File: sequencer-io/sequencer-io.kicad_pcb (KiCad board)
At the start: 2 copper layers, 156.5 x 89.8 mm, 96 parts, among them SW1 SW_Push, SW10 SW_Push, SW11 SW_Push, SW12 SW_Push, SW13 SW_Push, SW14 SW_Push, SW15 SW_Push, SW16 SW_Push, SW17 SW_Push, SW18 SW_Push, SW19 SW_Push, SW2 SW_Push, SW20 SW_Push, SW21 SW_Push, SW22 SW_Push, SW23 SW_Push, SW24 RotaryEncoder, SW3 SW_Push, SW4 SW_Push, SW5 SW_Push, SW6 SW_Push, SW7 SW_Push, SW8 SW_Push, SW9 SW_Push, U2 74HC595

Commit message: Edited PCB
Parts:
- added D24: 1N4148W, Diode_SMD:D_SOD-323_HandSoldering, B.Cu at (178.5, 115.5)
- added U20: SC0915, SC0915:SC0915, B.Cu at (155.8, 129.6)
- C10, C11, C12, C13, C14, C15, C16, C17, C18, C19, C20, C4, C5, C6, C7, C8, C9, U10, U11, U12, U13, U14, U15, U16, U17, U18, U19, U3, U4, U5, U6, U7, U8, U9: moved to B.Cu
- moved C13 173.3 mm to (38.1, 71.2), turned to 180 degrees
- moved C12 172.8 mm to (38.1, 90.5), turned to 180 degrees
- moved C14 154.6 mm to (57.1, 71.2), turned to 180 degrees
- moved C11 153.9 mm to (57.1, 90.5), turned to 180 degrees
- moved U3 138.7 mm to (171.5, 105.0), turned to 180 degrees
- moved C15 136.0 mm to (76.2, 71.2), turned to 180 degrees
- moved C10 135.1 mm to (76.2, 90.5), turned to 180 degrees
- moved C16 120.1 mm to (95.2, 71.2), turned to 180 degrees
- moved U4 115.3 mm to (171.4, 81.0), turned to 180 degrees
- moved U10 115.2 mm to (57.1, 81.0), turned to 180 degrees
- moved C9 111.2 mm to (95.2, 90.5), turned to 180 degrees
- moved C17 101.3 mm to (114.3, 71.2), turned to 180 degrees
- moved C8 92.2 mm to (114.3, 90.5), turned to 180 degrees
- moved C18 82.7 mm to (133.3, 71.2), turned to 180 degrees
- moved U9 77.6 mm to (76.2, 81.0), turned to 180 degrees
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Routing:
- net +5V: track 0.00 -> 616.1 mm, vias 0 -> 21
- net DIGIT_3: track 0.00 -> 267.2 mm
- net DIGIT_2: track 0.00 -> 261.2 mm
- net DIGIT_1: track 0.00 -> 246.4 mm
- net ENC_B: track 7.47 -> 200.8 mm
- net ENC_A: track 7.47 -> 197.7 mm
- net ROW1: track 133.4 -> 277.4 mm
- net ROW0: track 57.2 -> 164.7 mm
- net COL0: track 132.9 -> 238.0 mm, vias 0 -> 1
- net ROW3: track 128.4 -> 208.9 mm
- net COL3: track 105.1 -> 182.2 mm, vias 0 -> 1
- net ROW2: track 133.3 -> 209.5 mm
- net COL1: track 146.3 -> 213.3 mm, vias 0 -> 1
- net COL4: track 19.0 -> 85.8 mm, vias 0 -> 1
- net COL5: track 19.0 -> 70.7 mm, vias 0 -> 1
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- added copper zone on B.Cu, net GND
- added copper zone on F.Cu, net GND
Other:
- board size 156.5 x 89.8 mm -> 157 x 117 mm

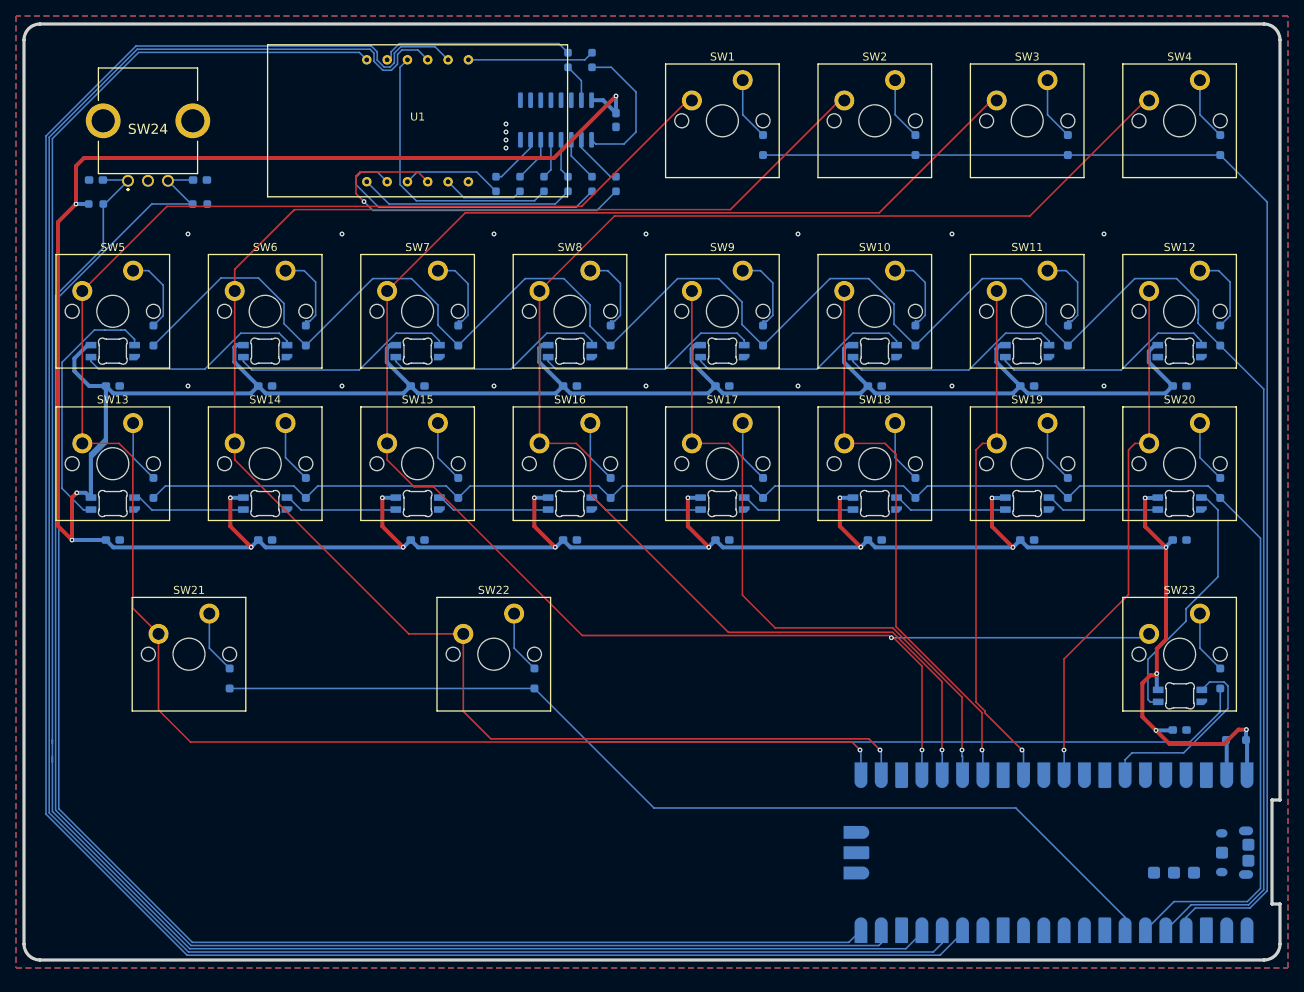
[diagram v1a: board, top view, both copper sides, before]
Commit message: Added TCA8418
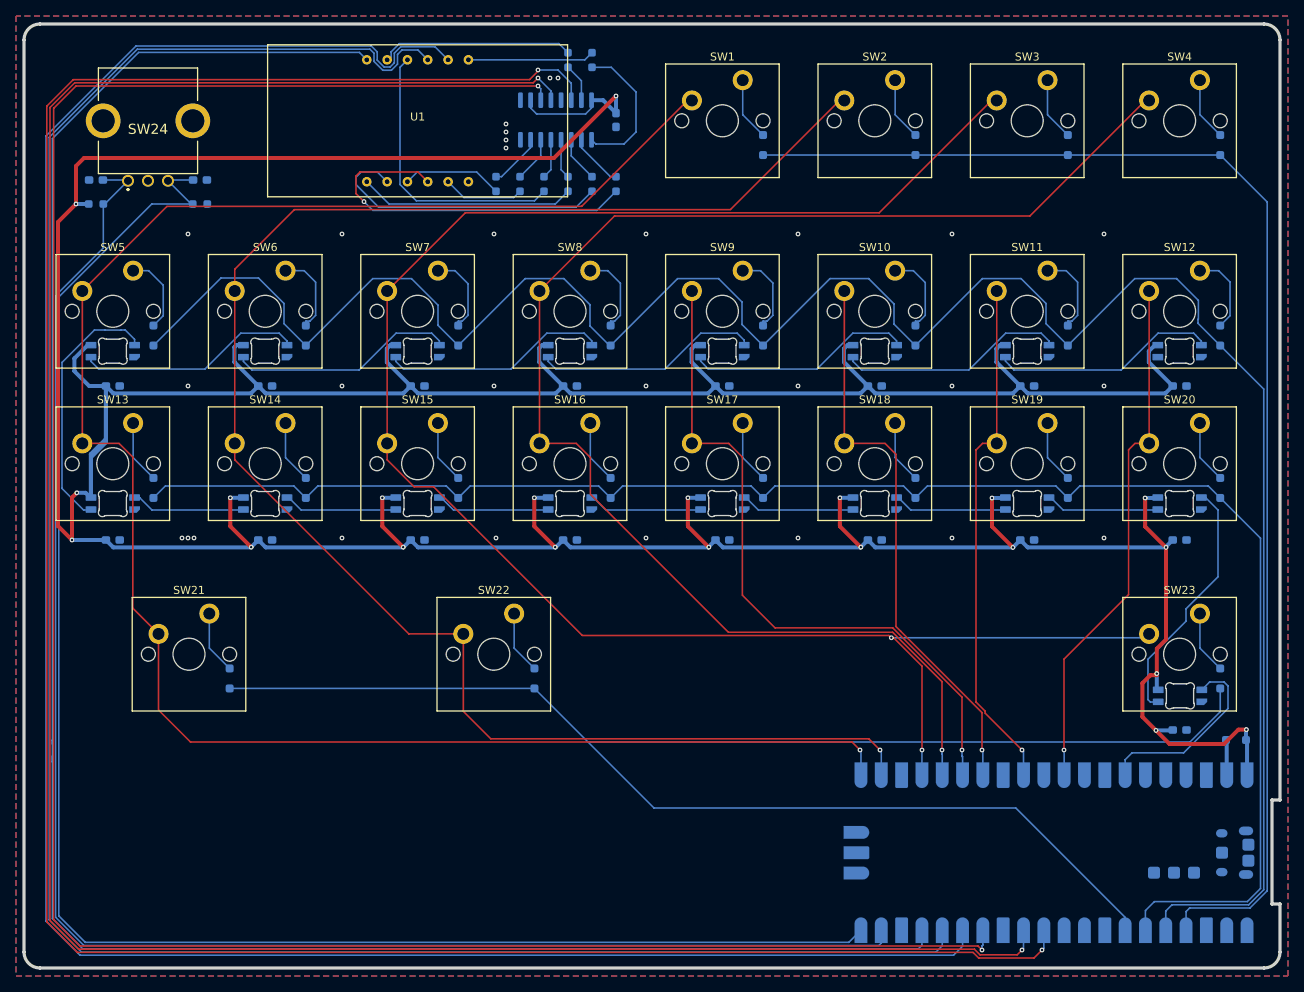
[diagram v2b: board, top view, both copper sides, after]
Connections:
- U2 pad 10: unconnected-(U2-~{SRCLR}-Pad10) -> +5V
- U2 pad 11: unconnected-(U2-SRCLK-Pad11) -> SRCLK
- U2 pad 12: unconnected-(U2-RCLK-Pad12) -> RCLK
- U2 pad 13: unconnected-(U2-~{OE}-Pad13) -> GND
- U2 pad 14: unconnected-(U2-SER-Pad14) -> SER
- U20 pad 11: unconnected-(U20-GP8-Pad11) -> SER
- U20 pad 12: unconnected-(U20-GP9-Pad12) -> RCLK
- U20 pad 14: unconnected-(U20-GP10-Pad14) -> SRCLK
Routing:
- net SER: track 0.00 -> 301.5 mm, vias 0 -> 2
- net RCLK: track 0.00 -> 293.7 mm, vias 0 -> 2
- net SRCLK: track 0.00 -> 285.2 mm, vias 0 -> 2
- net +5V: track 616.1 -> 626.3 mm
- net DIGIT_3: track 267.2 -> 276.0 mm
- net DIGIT_1: track 246.4 -> 255.2 mm
- net DIGIT_2: track 261.2 -> 269.2 mm
- net ENC_B: track 200.8 -> 208.7 mm
- net ENC_A: track 197.7 -> 205.5 mm
- net ROW2: track 209.5 -> 210.9 mm
- net ROW1: track 277.4 -> 278.8 mm
- net GND: vias 18 -> 29
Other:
- board size 157 x 117 mm -> 157 x 118 mm

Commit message: Added gitignore
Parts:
- added D25: BAT85, Package_TO_SOT_SMD:SOT-323_SC-70_Handsoldering, F.Cu at (133.5, 172.1)
- added D26: GATE, LED_THT:LED_D3.0mm_FlatTop, F.Cu at (126.3, 172.8)
- added J1: GateOut, Connector_PinHeader_2.54mm:PinHeader_1x02_P2.54mm_Vertical, F.Cu at (117.8, 165.2)
- added J2: ClockOut, Connector_PinHeader_2.54mm:PinHeader_1x02_P2.54mm_Vertical, F.Cu at (122.4, 165.2)
- added J3: PitchOut, Connector_PinHeader_2.54mm:PinHeader_1x02_P2.54mm_Vertical, F.Cu at (127.0, 165.2)
- added J4: CVOut, Connector_PinHeader_2.54mm:PinHeader_1x02_P2.54mm_Vertical, F.Cu at (131.7, 165.2)
- added J5: ClockIn, Connector_PinHeader_2.54mm:PinHeader_1x02_P2.54mm_Vertical, F.Cu at (136.3, 165.2)
- added J6: ResetIn, Connector_PinHeader_2.54mm:PinHeader_1x02_P2.54mm_Vertical, F.Cu at (141.0, 165.2)
- added Q1: MMBT3904, Package_TO_SOT_SMD:SOT-23, F.Cu at (122.2, 172.5)
- added Q2: MMBT3904, Package_TO_SOT_SMD:SOT-23, F.Cu at (122.2, 177.1)
- added R11: 1k, Resistor_SMD:R_0603_1608Metric_Pad0.98x0.95mm_HandSolder, F.Cu at (117.6, 171.3)
- added R12: 1k, Resistor_SMD:R_0603_1608Metric_Pad0.98x0.95mm_HandSolder, F.Cu at (117.6, 173.8)
- added R13: 100k, Resistor_SMD:R_0603_1608Metric_Pad0.98x0.95mm_HandSolder, F.Cu at (117.6, 176.4)
- added R14: 1M, Resistor_SMD:R_0603_1608Metric_Pad0.98x0.95mm_HandSolder, F.Cu at (117.6, 178.9)
- added R15: 10k, Resistor_SMD:R_0603_1608Metric_Pad0.98x0.95mm_HandSolder, F.Cu at (117.6, 181.4)
- added R16: 10k, Resistor_SMD:R_0603_1608Metric_Pad0.98x0.95mm_HandSolder, F.Cu at (117.6, 183.9)
- added R17: 100k, Resistor_SMD:R_0603_1608Metric_Pad0.98x0.95mm_HandSolder, F.Cu at (117.6, 186.4)
- added R18: 1M, Resistor_SMD:R_0603_1608Metric_Pad0.98x0.95mm_HandSolder, F.Cu at (117.6, 188.9)
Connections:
- U20 pad 1: unconnected-(U20-GP0-Pad1) -> GATE
- U20 pad 10: unconnected-(U20-GP7-Pad10) -> CV
- U20 pad 2: unconnected-(U20-GP1-Pad2) -> CLKOUT
- U20 pad 9: unconnected-(U20-GP6-Pad9) -> PITCH

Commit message: lil update
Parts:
- added C21: 100nF, Capacitor_SMD:C_0603_1608Metric_Pad1.08x0.95mm_HandSolder, F.Cu at (222.2, 76.9)
- added C22: 100nF, Capacitor_SMD:C_0603_1608Metric_Pad1.08x0.95mm_HandSolder, F.Cu at (222.2, 49.8)
- added C23: 22pF, Capacitor_SMD:C_0603_1608Metric_Pad1.08x0.95mm_HandSolder, F.Cu at (222.2, 52.3)
- added C24: 22pF, Capacitor_SMD:C_0603_1608Metric_Pad1.08x0.95mm_HandSolder, F.Cu at (222.2, 54.8)
- added C25: 100nF, Capacitor_SMD:C_0603_1608Metric_Pad1.08x0.95mm_HandSolder, F.Cu at (222.2, 57.3)
- added D27: SS34F, Diode_SMD:D_SMA_Handsoldering, F.Cu at (212.8, 61.0)
- added D28: 1SMB5918BT3G, Diode_SMD:D_SMB_Handsoldering, F.Cu at (212.8, 66.5)
- added IC1: TCA8418RTWR, Package_DFN_QFN:QFN-24-1EP_4x4mm_P0.5mm_EP2.5x2.5mm, B.Cu at (113.6, 105.2)
- added J7: ResetIn, Connector_PinHeader_2.54mm:PinHeader_1x02_P2.54mm_Vertical, F.Cu at (226.7, 77.9)
- added Q3: MMBT3906, Package_TO_SOT_SMD:SOT-23, F.Cu at (200.8, 60.6)
- added Q4: MMBT3906, Package_TO_SOT_SMD:SOT-23, F.Cu at (200.8, 65.2)
- added Q5: MMBT3904, Package_TO_SOT_SMD:SOT-23, F.Cu at (200.8, 69.8)
- added Q6: MMBT3904, Package_TO_SOT_SMD:SOT-23, F.Cu at (214.3, 99.4)
- added Q7: DMG2305UX-7, Package_TO_SOT_SMD:SOT-23, F.Cu at (226.9, 85.2)
- added R19: 680R, Resistor_SMD:R_0603_1608Metric_Pad0.98x0.95mm_HandSolder, F.Cu at (222.2, 79.4)
- added R20: 10k, Resistor_SMD:R_0603_1608Metric_Pad0.98x0.95mm_HandSolder, F.Cu at (222.2, 81.9)
- added R21: 1k, Resistor_SMD:R_0603_1608Metric_Pad0.98x0.95mm_HandSolder, B.Cu at (118.6, 108.4)
- added R22: 1k, Resistor_SMD:R_0603_1608Metric_Pad0.98x0.95mm_HandSolder, B.Cu at (121.6, 108.4)
- added R23: 100k, Resistor_SMD:R_0603_1608Metric_Pad0.98x0.95mm_HandSolder, F.Cu at (205.4, 59.5)
- added R24: 1M, Resistor_SMD:R_0603_1608Metric_Pad0.98x0.95mm_HandSolder, F.Cu at (205.4, 62.0)
- added R25: 10k, Resistor_SMD:R_0603_1608Metric_Pad0.98x0.95mm_HandSolder, F.Cu at (205.4, 64.5)
- added R26: 100k, Resistor_SMD:R_0603_1608Metric_Pad0.98x0.95mm_HandSolder, F.Cu at (205.4, 67.0)
- added R27: 1M, Resistor_SMD:R_0603_1608Metric_Pad0.98x0.95mm_HandSolder, F.Cu at (205.4, 69.5)
- added R28: 1k, Resistor_SMD:R_0603_1608Metric_Pad0.98x0.95mm_HandSolder, F.Cu at (222.2, 59.8)
- added R29: 10k, Resistor_SMD:R_0603_1608Metric_Pad0.98x0.95mm_HandSolder, F.Cu at (222.2, 62.3)
- added R30: 10k, Resistor_SMD:R_0603_1608Metric_Pad0.98x0.95mm_HandSolder, F.Cu at (222.2, 64.8)
- added R31: 1k, Resistor_SMD:R_0603_1608Metric_Pad0.98x0.95mm_HandSolder, F.Cu at (222.2, 67.3)
- added R32: 10k, Resistor_SMD:R_0603_1608Metric_Pad0.98x0.95mm_HandSolder, F.Cu at (222.2, 69.8)
- added R33: 10k, Resistor_SMD:R_0603_1608Metric_Pad0.98x0.95mm_HandSolder, F.Cu at (222.2, 72.3)
- added RV1: PITCH, Connector_PinHeader_2.54mm:PinHeader_1x03_P2.54mm_Vertical, F.Cu at (200.7, 50.8)
- added RV2: OCTAVE, Connector_PinHeader_2.54mm:PinHeader_1x03_P2.54mm_Vertical, F.Cu at (205.3, 50.8)
- added RV3: LENGTH, Connector_PinHeader_2.54mm:PinHeader_1x03_P2.54mm_Vertical, F.Cu at (210.0, 50.8)
- added RV4: CV, Connector_PinHeader_2.54mm:PinHeader_1x03_P2.54mm_Vertical, F.Cu at (214.6, 50.8)
- added TP1: TestPoint_Small, TestPoint:TestPoint_Pad_D1.0mm, B.Cu at (119.4, 111.6)
- added TP2: TestPoint_Small, TestPoint:TestPoint_Pad_D1.0mm, B.Cu at (117.2, 98.6)
- added TP3: TestPoint_Small, TestPoint:TestPoint_Pad_D1.0mm, B.Cu at (113.0, 111.6)
- added TP4: TestPoint_Small, TestPoint:TestPoint_Pad_D1.0mm, B.Cu at (114.0, 98.6)
- added TP5: TestPoint_Small, TestPoint:TestPoint_Pad_D1.0mm, B.Cu at (116.2, 111.6)
- added TP6: TestPoint_Small, TestPoint:TestPoint_Pad_D1.0mm, B.Cu at (109.8, 111.6)
- added U21: TL072, Package_SO:SOIC-8_3.9x4.9mm_P1.27mm, F.Cu at (228.6, 51.9)
- added U22: MCP4822, Package_SO:SOIC-8_3.9x4.9mm_P1.27mm, F.Cu at (228.6, 58.4)
- C1: value 100nF -> 47uF
- D1: value 1N4148W -> SS34F; footprint Diode_SMD:D_SOD-323_HandSoldering -> Diode_SMD:D_SMA_Handsoldering
- D25: value BAT85 -> 1SMB5918BT3G; footprint Package_TO_SOT_SMD:SOT-323_SC-70_Handsoldering -> Diode_SMD:D_SMB_Handsoldering
- J1: value GateOut -> 5V EXT
- J2: value ClockOut -> GateOut
- J3: value PitchOut -> ClockOut
- J4: value CVOut -> PitchOut
- J5: value ClockIn -> CVOut
- J6: value ResetIn -> ClockIn
- Q1: value MMBT3904 -> DMG2305UX-7
- Q2: value MMBT3904 -> MMBT3906
- R1, R2, R3, R4: value 100R -> 10k
- R10, R11, R12, R9: value 1k -> 100R
- R13: value 100k -> 100R
- R14: value 1M -> 100R
- R15, R16: value 10k -> 100R
- R17: value 100k -> 680R
- R18: value 1M -> 680R
- R5, R6, R7, R8: value 100R -> 1k
- U1: value ~ -> SC0915; footprint FJ5361BH:FJ5361BH -> SC0915:SC0915; moved to B.Cu
- U19: value ~ -> 74HC595; footprint SK6812MINI-E-012:SK6812MINI-E-012 -> Package_SO:SOIC-16_3.9x9.9mm_P1.27mm
- U2: value 74HC595 -> ~; footprint Package_SO:SOIC-16_3.9x9.9mm_P1.27mm -> SK6812MINI-E-012:SK6812MINI-E-012; moved to F.Cu
- U20: value SC0915 -> ~; footprint SC0915:SC0915 -> FJ5361BH:FJ5361BH
- moved D24 76.8 mm to (145.4, 184.8)
- moved U2 19.3 mm to (74.2, 38.0), turned to 0 degrees
- moved U1 17.2 mm to (93.4, 38.0), turned to 90 degrees
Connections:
- C2 pad 2: ENC_B -> +5V
- C20 pad 2: +5V -> /IOs/ENC_B
- C3 pad 2: ENC_A -> +5V
- D1 pad 1: ROW0 -> +5V
- D13 pad 1: ROW2 -> ROW1
- D21 pad 1: ROW3 -> ROW2
- D24 pad 1: /VSYS -> ROW3
- D24 pad 2: +5V -> Net-(D24-A)
- D25 pad 1: GATE -> /IOs/GATE
- D26 pad 2: GATE -> Net-(D26-A)
- D5 pad 1: ROW1 -> ROW0
- J1 pad 1: (no net) -> Net-(J1-Pin_1)
- J1 pad 2: (no net) -> GND
- Q1 pad 1: Net-(Q1-B) -> Net-(D1-A)
- Q1 pad 2: GND -> +5V
- Q1 pad 3: CLKIN -> Net-(J1-Pin_1)
- Q2 pad 2: GND -> +5V
- Q2 pad 3: RSTIN -> Net-(Q2-C)
- R1 pad 1: Net-(U2-QH) -> +3.3V
- R1 pad 2: Net-(U1-DP) -> /Switches/SDA
- R10 pad 1: +5V -> Net-(U19-QB)
- R10 pad 2: ENC_A -> Net-(U20-B)
- R11 pad 1: GATE -> Net-(U19-QC)
- R11 pad 2: Net-(J1-PadT) -> Net-(U20-C)
- R12 pad 1: GND -> Net-(U19-QD)
- R12 pad 2: Net-(D26-K) -> Net-(U20-D)
- R13 pad 1: Net-(J5-PadT) -> Net-(U19-QE)
- R13 pad 2: Net-(Q1-B) -> Net-(U20-E)
- R14 pad 1: GND -> Net-(U19-QF)
- R14 pad 2: Net-(Q1-B) -> Net-(U20-F)
- R15 pad 1: CLKIN -> Net-(U19-QG)
- R15 pad 2: +5V -> Net-(U20-G)
- R16 pad 1: RSTIN -> Net-(U19-QH)
- R16 pad 2: +5V -> Net-(U20-DP)
- R17 pad 1: Net-(J6-PadT) -> Net-(Q2-B)
- R17 pad 2: Net-(Q2-B) -> /IOs/DIGIT_1
- R18 pad 1: GND -> Net-(Q3-B)
- R18 pad 2: Net-(Q2-B) -> /IOs/DIGIT_2
- R2 pad 1: Net-(U2-QG) -> +3.3V
- R2 pad 2: Net-(U1-G) -> /Switches/SCL
- R3 pad 1: Net-(U2-QF) -> +3.3V
- R3 pad 2: Net-(U1-F) -> Net-(IC1-~{INT})
- R4 pad 1: Net-(U2-QE) -> +3.3V
- R4 pad 2: Net-(U1-E) -> Net-(IC1-~{RESET})
- R5 pad 1: Net-(U2-QD) -> Net-(D26-A)
- R5 pad 2: Net-(U1-D) -> /IOs/GATE
- R6 pad 1: Net-(U2-QC) -> GND
- R6 pad 2: Net-(U1-C) -> Net-(D26-K)
- R7 pad 1: Net-(U2-QB) -> Net-(D26-A)
- R7 pad 2: Net-(U1-B) -> Net-(J2-PadT)
- R8 pad 1: Net-(U2-QA) -> Net-(J3-PadT)
- R8 pad 2: Net-(U1-A) -> /IOs/CLKOUT
- R9 pad 1: +5V -> Net-(U19-QA)
- R9 pad 2: ENC_B -> Net-(U20-A)
- SW1 pad 2: Net-(D1-A) -> Net-(D2-A)
- SW10 pad 2: Net-(D10-A) -> Net-(D11-A)
- SW11 pad 2: Net-(D11-A) -> Net-(D12-A)
- SW12 pad 2: Net-(D12-A) -> Net-(D13-A)
- SW13 pad 2: Net-(D13-A) -> Net-(D14-A)
- SW14 pad 2: Net-(D14-A) -> Net-(D15-A)
- SW15 pad 2: Net-(D15-A) -> Net-(D16-A)
- SW16 pad 2: Net-(D16-A) -> Net-(D17-A)
- SW17 pad 2: Net-(D17-A) -> Net-(D18-A)
- SW18 pad 2: Net-(D18-A) -> Net-(D19-A)
- SW19 pad 2: Net-(D19-A) -> Net-(D20-A)
- SW2 pad 2: Net-(D2-A) -> Net-(D3-A)
- SW20 pad 2: Net-(D20-A) -> Net-(D21-A)
- SW21 pad 2: Net-(D21-A) -> Net-(D22-A)
- SW22 pad 2: Net-(D22-A) -> Net-(D23-A)
- SW23 pad 2: Net-(D23-A) -> Net-(D24-A)
- SW24 pad A: ENC_A -> /IOs/ENC_A
- SW24 pad B: ENC_B -> /IOs/ENC_B
- SW3 pad 2: Net-(D3-A) -> Net-(D4-A)
- SW4 pad 2: Net-(D4-A) -> Net-(D5-A)
- SW5 pad 2: Net-(D5-A) -> Net-(D6-A)
- SW6 pad 2: Net-(D6-A) -> Net-(D7-A)
- SW7 pad 2: Net-(D7-A) -> Net-(D8-A)
- SW8 pad 2: Net-(D8-A) -> Net-(D9-A)
- SW9 pad 2: Net-(D9-A) -> Net-(D10-A)
- U1 pad 1: Net-(U1-E) -> /Switches/SDA
- U1 pad 10: Net-(U1-F) -> unconnected-(U1-GP7-Pad10)
- U1 pad 11: Net-(U1-A) -> unconnected-(U1-GP8-Pad11)
- U1 pad 12: DIGIT_1 -> unconnected-(U1-GP9-Pad12)
- U1 pad 2: Net-(U1-D) -> /Switches/SCL
- U1 pad 3: Net-(U1-DP) -> GND
- U1 pad 4: Net-(U1-C) -> unconnected-(U1-GP2-Pad4)
- U1 pad 5: Net-(U1-G) -> unconnected-(U1-GP3-Pad5)
- U1 pad 7: Net-(U1-B) -> unconnected-(U1-GP5-Pad7)
- U1 pad 8: DIGIT_3 -> GND
- U1 pad 9: DIGIT_2 -> unconnected-(U1-GP6-Pad9)
- U18 pad 4: Net-(U18-DOUT) -> unconnected-(U18-DOUT-Pad4)
- U19 pad 1: GND -> Net-(U19-QB)
- U19 pad 2: Net-(U18-DOUT) -> Net-(U19-QC)
- U19 pad 3: +5V -> Net-(U19-QD)
- U19 pad 4: unconnected-(U19-DOUT-Pad4) -> Net-(U19-QE)
- U2 pad 1: Net-(U2-QB) -> GND
- U2 pad 2: Net-(U2-QC) -> /LEDs/PXL
- U2 pad 3: Net-(U2-QD) -> +5V
- U2 pad 4: Net-(U2-QE) -> Net-(U2-DOUT)
- U20 pad 1: GATE -> Net-(U20-E)
- U20 pad 10: CV -> Net-(U20-F)
- U20 pad 11: SER -> Net-(U20-A)
- U20 pad 12: RCLK -> Net-(Q2-C)
- U20 pad 2: CLKOUT -> Net-(U20-D)
- U20 pad 3: GND -> Net-(U20-DP)
- U20 pad 4: ROW0 -> Net-(U20-C)
- U20 pad 5: ROW1 -> Net-(U20-G)
- U20 pad 6: ROW2 -> unconnected-(U20-NC-Pad6)
- U20 pad 7: ROW3 -> Net-(U20-B)
- U20 pad 8: GND -> Net-(Q4-C)
- U20 pad 9: PITCH -> Net-(Q3-C)
- U3 pad 2: PXL -> Net-(U2-DOUT)
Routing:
- net +5V: track 626.3 -> 0.00 mm, vias 21 -> 0
- net SER: track 301.5 -> 0.00 mm, vias 2 -> 0
- net RCLK: track 293.7 -> 0.00 mm, vias 2 -> 0
- net SRCLK: track 285.2 -> 0.00 mm, vias 2 -> 0
- net ROW1: track 278.8 -> 0.00 mm
- net DIGIT_3: track 276.0 -> 0.00 mm
- net DIGIT_2: track 269.2 -> 0.00 mm
- net DIGIT_1: track 255.2 -> 0.00 mm
- net COL2: track 230.8 -> 19.0 mm, vias 2 -> 0
- net ROW2: track 210.9 -> 0.00 mm
- net ROW3: track 208.9 -> 0.00 mm
- net ENC_B: track 208.7 -> 0.00 mm
- net ENC_A: track 205.5 -> 0.00 mm
- net COL0: track 238.0 -> 46.8 mm, vias 1 -> 0
- net ROW0: track 165.1 -> 0.00 mm
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
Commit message: edits
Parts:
- removed Q6: MMBT3904, Package_TO_SOT_SMD:SOT-23
- C1: value 47uF -> 100nF; moved to F.Cu
- C2, C3: moved to F.Cu
- C21: value 100nF -> 47uF
- C22: value 100nF -> 22pF
- C24: value 22pF -> 100nF
- D1: value SS34F -> 1N4148W; footprint Diode_SMD:D_SMA_Handsoldering -> Diode_SMD:D_SOD-323_HandSoldering
- D24: value 1N4148W -> SS34F; footprint Diode_SMD:D_SOD-323_HandSoldering -> Diode_SMD:D_SMA_Handsoldering; moved to F.Cu
- D25: value 1SMB5918BT3G -> GATE; footprint Diode_SMD:D_SMB_Handsoldering -> LED_THT:LED_D3.0mm_FlatTop
- D26: value GATE -> SS34F; footprint LED_THT:LED_D3.0mm_FlatTop -> Diode_SMD:D_SMA_Handsoldering
- D27: value SS34F -> 1SMB5918BT3G; footprint Diode_SMD:D_SMA_Handsoldering -> Diode_SMD:D_SMB_Handsoldering
- J1: value 5V EXT -> ClockIn
- J6: value ClockIn -> ResetIn
- J7: value ResetIn -> 5V EXT
- Q1: value DMG2305UX-7 -> MMBT3904
- Q2: value MMBT3906 -> MMBT3904
- Q5: value MMBT3904 -> MMBT3906
- R1, R2, R3, R4: value 10k -> 100R; moved to F.Cu
- R10: value 100R -> 1k; moved to F.Cu
- R11, R12, R15: value 100R -> 1k
- R13: value 100R -> 100k
- R14: value 100R -> 1M
- R16: value 100R -> 10k
- R17: value 680R -> 100k
- R18: value 680R -> 1M
- R19: value 680R -> 10k
- R21, R22, R31: value 1k -> 10k
- R23: value 100k -> 680R
- R24: value 1M -> 680R
- R25: value 10k -> 680R
- R26: value 100k -> 1k
- R27: value 1M -> 1k
- R30: value 10k -> 1k
- R5, R6, R7, R8: value 1k -> 100R; moved to F.Cu
- R9: value 100R -> 10k; moved to F.Cu
- U1: value SC0915 -> 74HC595; footprint SC0915:SC0915 -> Package_SO:SOIC-16_3.9x9.9mm_P1.27mm; moved to F.Cu
- U12, U13, U14, U15, U16, U17, U18: footprint SK6812MINI-E-012:SK6812MINI-E-012 -> SK6812MINI-E-012:SK6812MINI-E-012-ROT
- U19: value 74HC595 -> ~; footprint Package_SO:SOIC-16_3.9x9.9mm_P1.27mm -> SK6812MINI-E-012:SK6812MINI-E-012-ROT
- U2: footprint SK6812MINI-E-012:SK6812MINI-E-012 -> FJ5361BH:FJ5361BH
- U20: value ~ -> SC0915; footprint FJ5361BH:FJ5361BH -> SC0915:SC0915; moved to F.Cu
- U21: value TL072 -> MCP4822
- U22: value MCP4822 -> TL072
- moved R10 231.0 mm to (265.5, 74.5)
- moved C3 226.2 mm to (261.2, 66.9)
- moved R9 217.8 mm to (265.5, 72.0), turned to 0 degrees
- moved C2 213.0 mm to (261.2, 64.4), turned to 0 degrees
- moved SW24 208.5 mm to (249.7, 61.6)
- moved D24 195.7 mm to (284.0, 46.7)
- moved U1 194.2 mm to (285.5, 66.6), turned to 0 degrees
- moved Q1 191.1 mm to (278.9, 63.1)
- moved Q2 191.1 mm to (278.9, 67.7)
- moved R12 189.0 mm to (269.9, 61.9)
- moved R13 189.0 mm to (269.9, 64.4)
- moved R14 189.0 mm to (269.9, 66.9)
- moved R15 189.0 mm to (269.9, 69.4)
- moved R16 189.0 mm to (269.9, 72.0)
- moved R17 189.0 mm to (269.9, 74.5)
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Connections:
- C2 pad 2: +5V -> /IOs/ENC_B
- C20 pad 2: /IOs/ENC_B -> +5V
- C21 pad 2: /IOs/ENC_A -> +5V
- C22 pad 1: GND -> Net-(U22A--)
- C22 pad 2: +5V -> Net-(C22-Pad2)
- C23 pad 1: Net-(U21A--) -> Net-(U22B--)
- C24 pad 1: Net-(U21B--) -> GND
- C24 pad 2: Net-(C24-Pad2) -> +5V
- C3 pad 2: +5V -> /IOs/ENC_A
- D1 pad 1: +5V -> ROW0
- D13 pad 1: ROW1 -> ROW2
- D21 pad 1: ROW2 -> ROW3
- D24 pad 1: ROW3 -> Net-(D24-K)
- D24 pad 2: Net-(D24-A) -> GND
- D25 pad 1: /IOs/GATE -> Net-(D25-K)
- D25 pad 2: GND -> Net-(D24-K)
- D26 pad 1: Net-(D26-K) -> +5V
- D27 pad 1: Net-(D26-A) -> /IOs/GATE
- D5 pad 1: ROW0 -> ROW1
- J1 pad 1: Net-(J1-Pin_1) -> (no net)
- J1 pad 2: GND -> (no net)
- J7 pad 1: (no net) -> Net-(J7-Pin_1)
- J7 pad 2: (no net) -> GND
- Q1 pad 1: Net-(D1-A) -> Net-(Q1-B)
- Q1 pad 2: +5V -> GND
- Q1 pad 3: Net-(J1-Pin_1) -> /IOs/CLKIN
- Q2 pad 2: +5V -> GND
- Q2 pad 3: Net-(Q2-C) -> /IOs/RSTIN
- Q5 pad 2: GND -> +5V
- Q5 pad 3: /IOs/CLKIN -> Net-(Q5-C)
- R1 pad 1: +3.3V -> Net-(U1-QA)
- R1 pad 2: /Switches/SDA -> Net-(U2-A)
- R10 pad 1: Net-(U19-QB) -> GND
- R10 pad 2: Net-(U20-B) -> Net-(D25-K)
- R11 pad 1: Net-(U19-QC) -> +5V
- R11 pad 2: Net-(U20-C) -> /IOs/ENC_A
- R12 pad 1: Net-(U19-QD) -> +5V
- R12 pad 2: Net-(U20-D) -> /IOs/ENC_B
- R13 pad 1: Net-(U19-QE) -> Net-(J1-PadT)
- R13 pad 2: Net-(U20-E) -> Net-(Q1-B)
- R14 pad 1: Net-(U19-QF) -> GND
- R14 pad 2: Net-(U20-F) -> Net-(Q1-B)
- R15 pad 1: Net-(U19-QG) -> Net-(D24-K)
- R15 pad 2: Net-(U20-G) -> Net-(J2-PadT)
- R16 pad 1: Net-(U19-QH) -> /IOs/RSTIN
- R16 pad 2: Net-(U20-DP) -> +5V
- R17 pad 1: Net-(Q2-B) -> Net-(J6-PadT)
- R17 pad 2: /IOs/DIGIT_1 -> Net-(Q2-B)
- R18 pad 1: Net-(Q3-B) -> GND
- R18 pad 2: /IOs/DIGIT_2 -> Net-(Q2-B)
- R19 pad 1: Net-(Q4-B) -> +3.3V
- R19 pad 2: /IOs/DIGIT_3 -> /Switches/SDA
- R2 pad 1: +3.3V -> Net-(U1-QB)
- R2 pad 2: /Switches/SCL -> Net-(U2-B)
- R20 pad 1: /IOs/CLKIN -> +3.3V
- R20 pad 2: +5V -> /Switches/SCL
- R21 pad 1: +5V -> +3.3V
- R21 pad 2: /IOs/ENC_A -> Net-(IC1-~{INT})
- R22 pad 1: +5V -> +3.3V
- R22 pad 2: /IOs/ENC_B -> Net-(IC1-~{RESET})
- R23 pad 1: Net-(J6-PadT) -> Net-(Q5-B)
- R23 pad 2: Net-(Q5-B) -> /IOs/DIGIT_1
- R24 pad 1: GND -> Net-(Q4-B)
- R24 pad 2: Net-(Q5-B) -> /IOs/DIGIT_2
- R25 pad 1: /IOs/RSTIN -> Net-(Q3-B)
- R25 pad 2: +5V -> /IOs/DIGIT_3
- R26 pad 1: Net-(J7-PadT) -> Net-(D24-K)
- R26 pad 2: Net-(Q6-B) -> /IOs/GATE
- R27 pad 1: GND -> Net-(J3-PadT)
- R27 pad 2: Net-(Q6-B) -> /IOs/CLKOUT
- R28 pad 1: Net-(C23-Pad2) -> Net-(C22-Pad2)
- R29 pad 1: GND -> Net-(U22A--)
- R29 pad 2: Net-(U21A--) -> /DAC/PITCH
- R3 pad 1: +3.3V -> Net-(U1-QC)
- R3 pad 2: Net-(IC1-~{INT}) -> Net-(U2-C)
- R30 pad 1: Net-(U21A--) -> Net-(C23-Pad2)
- R30 pad 2: /DAC/PITCH -> /DAC/CV
- R31 pad 1: Net-(C24-Pad2) -> Net-(U22B--)
- R32 pad 2: Net-(U21B--) -> Net-(U22B--)
- R33 pad 1: Net-(U21B--) -> GND
- R33 pad 2: /DAC/CV -> Net-(U22A--)
- R4 pad 1: +3.3V -> Net-(U1-QD)
- R4 pad 2: Net-(IC1-~{RESET}) -> Net-(U2-D)
- R5 pad 1: Net-(D26-A) -> Net-(U1-QE)
- R5 pad 2: /IOs/GATE -> Net-(U2-E)
- R6 pad 1: GND -> Net-(U1-QF)
- R6 pad 2: Net-(D26-K) -> Net-(U2-F)
- R7 pad 1: Net-(D26-A) -> Net-(U1-QG)
- R7 pad 2: Net-(J2-PadT) -> Net-(U2-G)
- R8 pad 1: Net-(J3-PadT) -> Net-(U1-QH)
- R8 pad 2: /IOs/CLKOUT -> Net-(U2-DP)
- R9 pad 1: Net-(U19-QA) -> /IOs/CLKIN
- R9 pad 2: Net-(U20-A) -> +5V
- SW1 pad 2: Net-(D2-A) -> Net-(D1-A)
- SW10 pad 2: Net-(D11-A) -> Net-(D10-A)
- SW11 pad 2: Net-(D12-A) -> Net-(D11-A)
- SW12 pad 2: Net-(D13-A) -> Net-(D12-A)
- SW13 pad 2: Net-(D14-A) -> Net-(D13-A)
- SW14 pad 2: Net-(D15-A) -> Net-(D14-A)
- SW15 pad 2: Net-(D16-A) -> Net-(D15-A)
- SW16 pad 2: Net-(D17-A) -> Net-(D16-A)
- SW17 pad 2: Net-(D18-A) -> Net-(D17-A)
- SW18 pad 2: Net-(D19-A) -> Net-(D18-A)
- SW19 pad 2: Net-(D20-A) -> Net-(D19-A)
- SW2 pad 2: Net-(D3-A) -> Net-(D2-A)
- SW20 pad 2: Net-(D21-A) -> Net-(D20-A)
- SW21 pad 2: Net-(D22-A) -> Net-(D21-A)
- SW22 pad 2: Net-(D23-A) -> Net-(D22-A)
- SW23 pad 2: Net-(D24-A) -> Net-(D23-A)
- SW3 pad 2: Net-(D4-A) -> Net-(D3-A)
- SW4 pad 2: Net-(D5-A) -> Net-(D4-A)
- SW5 pad 2: Net-(D6-A) -> Net-(D5-A)
- SW6 pad 2: Net-(D7-A) -> Net-(D6-A)
- SW7 pad 2: Net-(D8-A) -> Net-(D7-A)
- SW8 pad 2: Net-(D9-A) -> Net-(D8-A)
- SW9 pad 2: Net-(D10-A) -> Net-(D9-A)
- U1 pad 1: /Switches/SDA -> Net-(U1-QB)
- U1 pad 10: unconnected-(U1-GP7-Pad10) -> +5V
- U1 pad 11: unconnected-(U1-GP8-Pad11) -> /DAC/SCLK
- U1 pad 12: unconnected-(U1-GP9-Pad12) -> /IOs/CS_SHIFT
- U1 pad 14: unconnected-(U1-GP10-Pad14) -> /IOs/SER
- U1 pad 15: unconnected-(U1-GP11-Pad15) -> Net-(U1-QA)
- U1 pad 16: unconnected-(U1-GP12-Pad16) -> +5V
- U1 pad 2: /Switches/SCL -> Net-(U1-QC)
- U1 pad 3: GND -> Net-(U1-QD)
- U1 pad 4: unconnected-(U1-GP2-Pad4) -> Net-(U1-QE)
- U1 pad 5: unconnected-(U1-GP3-Pad5) -> Net-(U1-QF)
- U1 pad 6: unconnected-(U1-GP4-Pad6) -> Net-(U1-QG)
- U1 pad 7: unconnected-(U1-GP5-Pad7) -> Net-(U1-QH)
- U18 pad 4: unconnected-(U18-DOUT-Pad4) -> Net-(U18-DOUT)
- U19 pad 1: Net-(U19-QB) -> GND
- U19 pad 2: Net-(U19-QC) -> Net-(U18-DOUT)
- U19 pad 3: Net-(U19-QD) -> +5V
- U19 pad 4: Net-(U19-QE) -> unconnected-(U19-DOUT-Pad4)
- U2 pad 1: GND -> Net-(U2-E)
- U2 pad 2: /LEDs/PXL -> Net-(U2-D)
- U2 pad 3: +5V -> Net-(U2-DP)
- U2 pad 4: Net-(U2-DOUT) -> Net-(U2-C)
- U20 pad 1: Net-(U20-E) -> /Switches/SDA
- U20 pad 10: Net-(U20-F) -> unconnected-(U20-GP7-Pad10)
- U20 pad 11: Net-(U20-A) -> unconnected-(U20-GP8-Pad11)
- U20 pad 12: Net-(Q2-C) -> unconnected-(U20-GP9-Pad12)
- U20 pad 2: Net-(U20-D) -> /Switches/SCL
- U20 pad 3: Net-(U20-DP) -> GND
- U20 pad 4: Net-(U20-C) -> unconnected-(U20-GP2-Pad4)
- U20 pad 5: Net-(U20-G) -> unconnected-(U20-GP3-Pad5)
- U20 pad 7: Net-(U20-B) -> unconnected-(U20-GP5-Pad7)
- U20 pad 8: Net-(Q4-C) -> GND
- U20 pad 9: Net-(Q3-C) -> unconnected-(U20-GP6-Pad9)
- U21 pad 1: Net-(C23-Pad2) -> +5V
- U21 pad 2: Net-(U21A--) -> /DAC/CS_DAC
- U21 pad 3: Net-(U21A-+) -> /DAC/SCLK
- U21 pad 4: -12V -> /DAC/MOSI
- U21 pad 5: Net-(U21B-+) -> GND
- U21 pad 6: Net-(U21B--) -> Net-(U21-VB)
- U21 pad 7: Net-(C24-Pad2) -> GND
- U21 pad 8: +12V -> Net-(U21-VA)
- U22 pad 1: +5V -> Net-(C22-Pad2)
- U22 pad 2: /DAC/CS_DAC -> Net-(U22A--)
- U22 pad 3: /DAC/SCLK -> Net-(U21-VA)
- U22 pad 4: /DAC/MOSI -> -12V
- U22 pad 5: GND -> Net-(U21-VB)
- U22 pad 6: Net-(U21B-+) -> Net-(U22B--)
- U22 pad 7: GND -> Net-(C23-Pad2)
- U22 pad 8: Net-(U21A-+) -> +12V
- U3 pad 2: Net-(U2-DOUT) -> /LEDs/PXL
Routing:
- net ROW1: track 0.00 -> 216.4 mm, vias 0 -> 2
- net ROW2: track 0.00 -> 189.9 mm, vias 0 -> 2
- net ROW3: track 0.00 -> 159.7 mm
- net ROW0: track 0.00 -> 124.8 mm, vias 0 -> 2
- net COL0: track 46.8 -> 136.6 mm
- net COL7: track 19.0 -> 85.5 mm, vias 0 -> 1
- net COL2: track 19.0 -> 84.5 mm, vias 0 -> 1
- net COL6: track 19.0 -> 66.2 mm, vias 0 -> 1
- net COL3: track 19.0 -> 64.9 mm, vias 0 -> 1
- net Net-(U3-DOUT): track 29.4 -> 0.00 mm
- net COL5: track 19.0 -> 47.4 mm, vias 0 -> 1
- net COL4: track 19.0 -> 47.2 mm, vias 0 -> 1
- net GND: track 0.00 -> 16.8 mm, vias 0 -> 9
- net Net-(U18-DOUT): track 28.5 -> 14.9 mm
- net Net-(U13-DOUT): track 28.5 -> 14.9 mm
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- removed copper zone on B.Cu, net GND
- removed copper zone on F.Cu, net GND
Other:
- board size 157 x 118 mm -> 3.6 x 3.3 mm
